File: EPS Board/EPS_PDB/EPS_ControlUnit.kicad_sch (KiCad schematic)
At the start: 35 parts, among them Q1 PMOS, Q2 NMOS, SW1 SW_SPDT, U2 MCP2551-I-P, U3 MCP2551-I-P, U4 STM32L476VET6, U5 TPS3824-33QDBVRQ1, Y1 32MHz

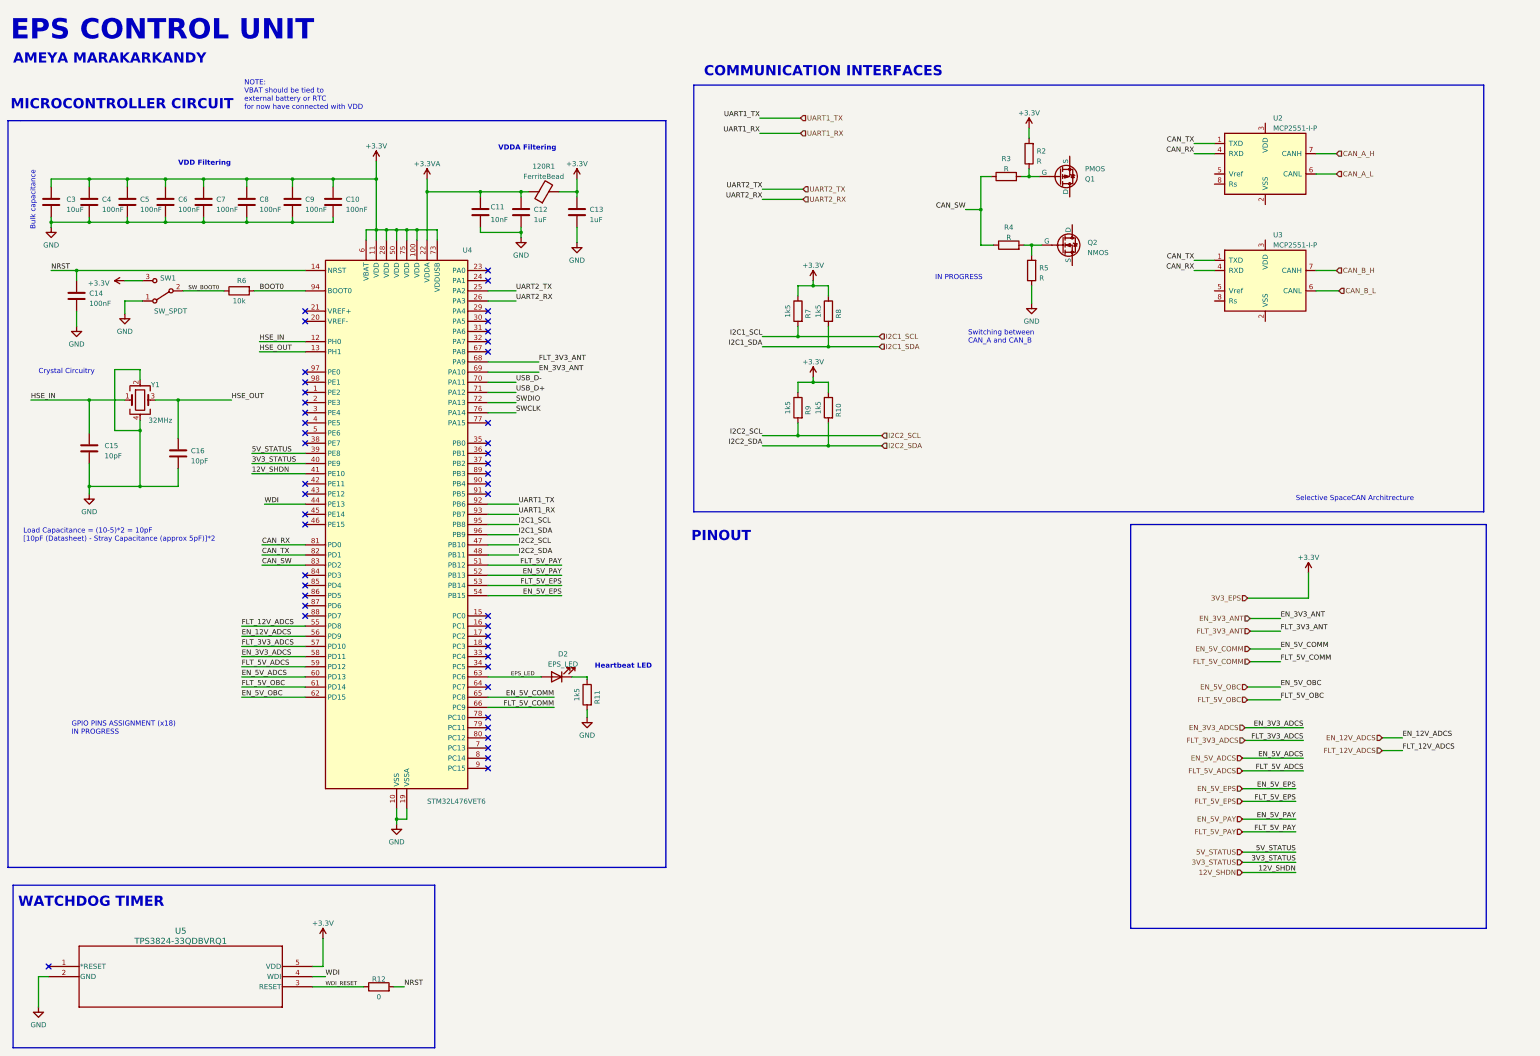
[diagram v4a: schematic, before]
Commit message: completed CAN transceiver switching circuit
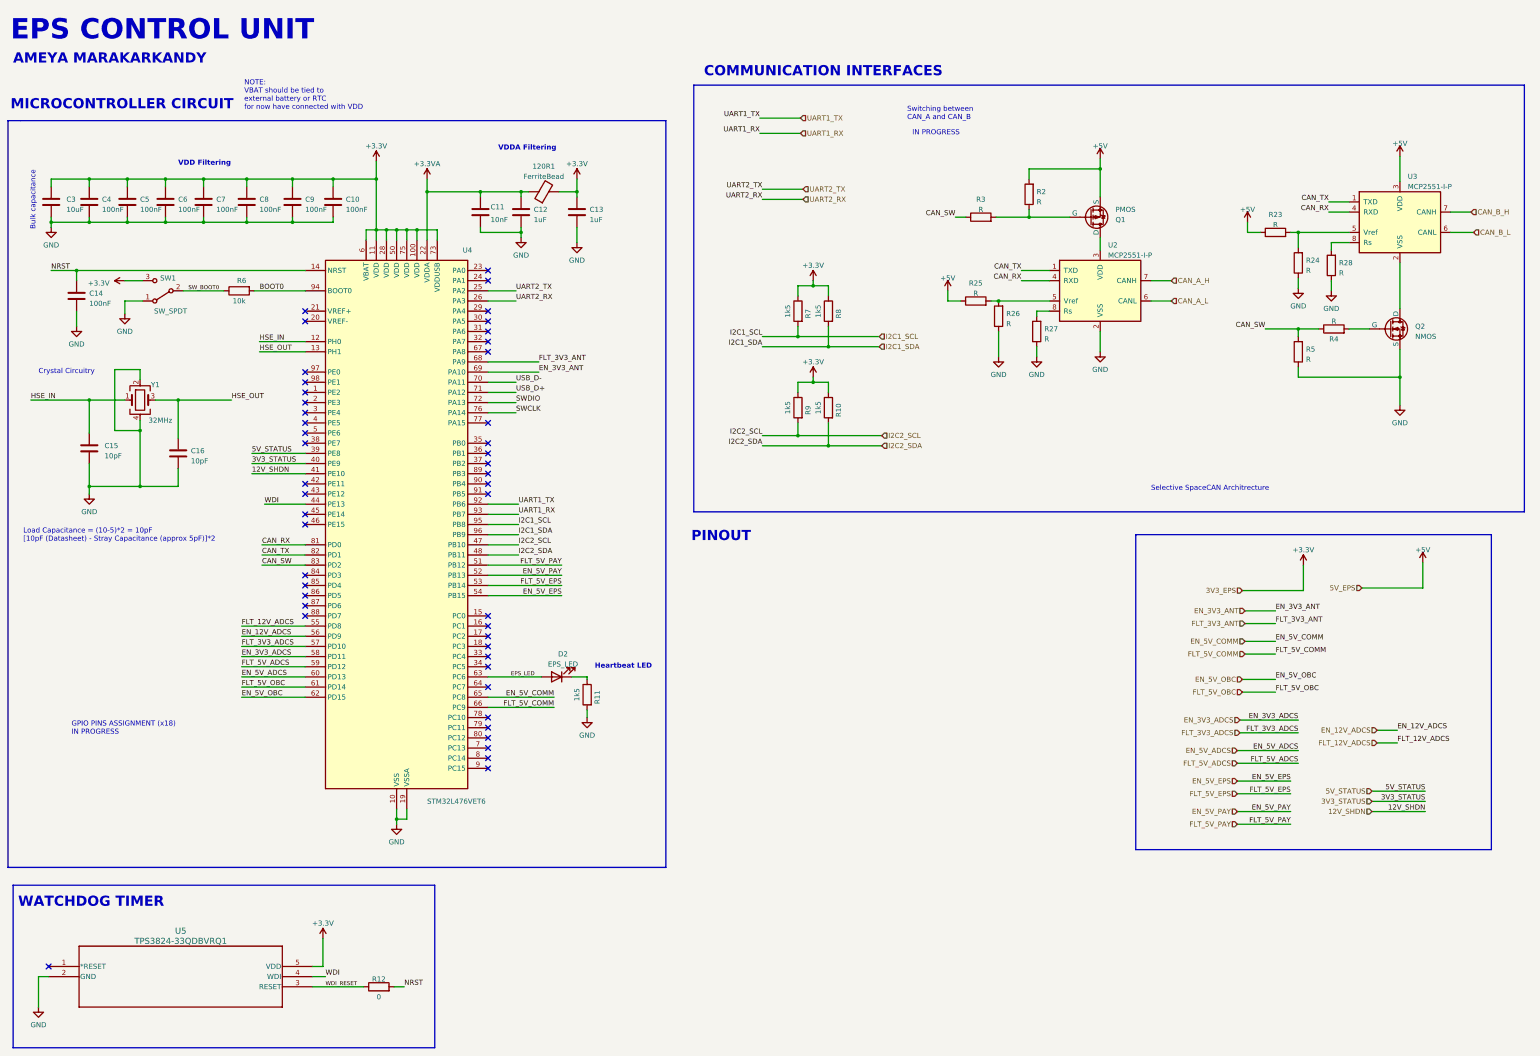
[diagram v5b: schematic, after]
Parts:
- added R23, R24, R25, R26, R27, R28: R, symbol Device:R
- U2, U3: footprint Package_DIP:DIP-8_W7.62mm -> Package_SO:SOIC-8_3.9x4.9mm_P1.27mm; symbol Interface_CAN_LIN:MCP2551-I-P -> Interface_CAN_LIN:MCP2551-I-SN
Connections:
- net +3.3V: no longer R2.2
- net CAN_SW: now also R5.2
- net GND: now also Q2.3 (S), U2.2 (VSS), R24.1, R26.1, R27.1, R28.1
- net at U3.2 (VSS): now also Q2.1 (D)
- net +5V: now reaches U3.3 (VDD)
- net +5V: now also Q1.3 (S), R2.2, R23.1, R25.1
- net at U3.5 (Vref): now also R23.2, R24.2
- net at U3.8 (Rs): now also R28.2
- net at Q1.1 (D): now also U2.3 (VDD)
- net at U2.5 (Vref): now also R25.2, R26.2
- net at U2.8 (Rs): now also R27.2
- net at Q2.2 (G), R4.2: no longer R5.2
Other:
- company: (none) -> IIT Bombay Student Satellite Program
- title: (none) -> EPS Control Unit
- moved on the sheet: Q1, Q2, R2, R3, R4, R5, U2, U3
